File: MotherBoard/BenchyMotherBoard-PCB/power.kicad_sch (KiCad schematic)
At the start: 158 parts, among them J1 PWR-CONN, U1 TPS65400RGZT, U10 USB7206C, U11 AP2127K-3.3, U2 STM32MP157FAB1, U3 MAX15027, U4 TPS7A94, U5 ATTINY416-MNR, U6 SN74LVC1G32, U7 MAX15027, U8 74HCT2G08, U9 MAX15027

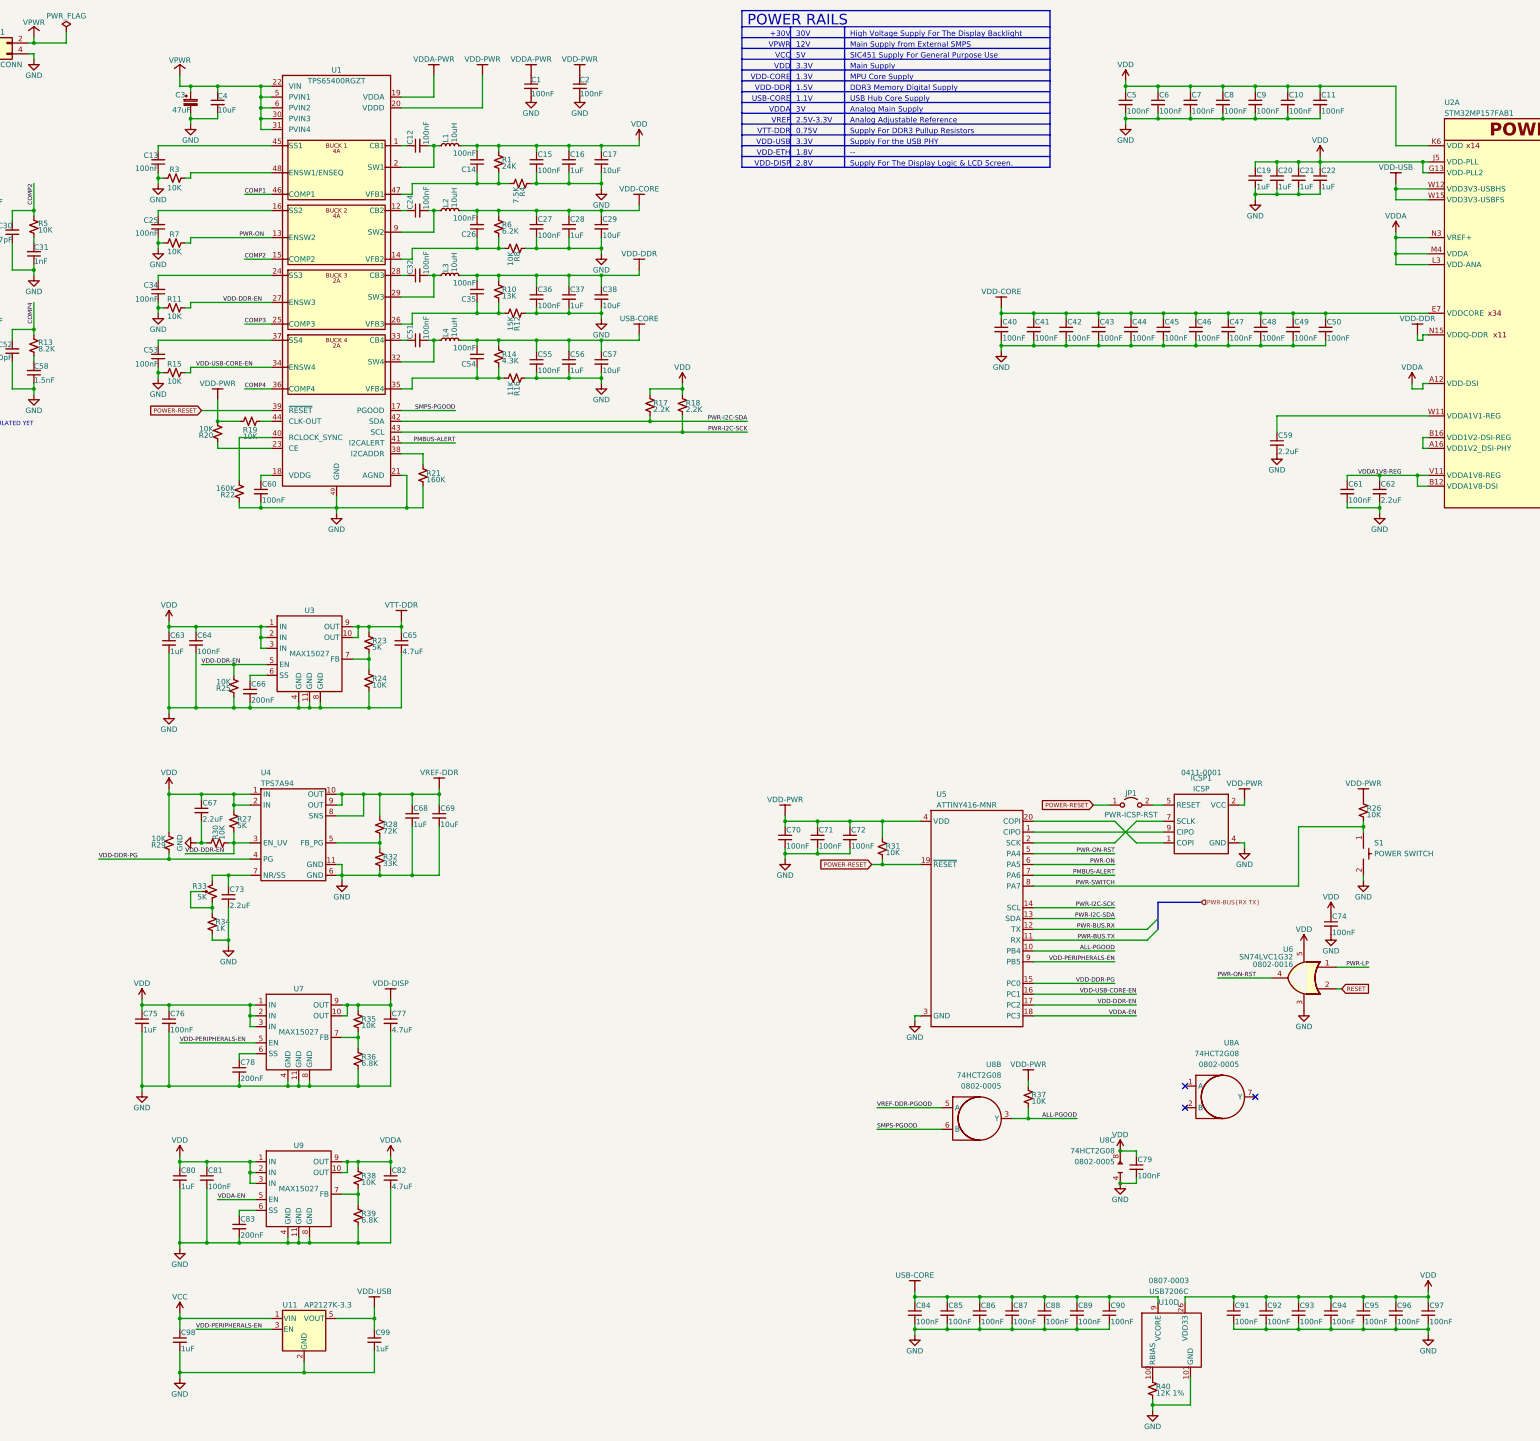
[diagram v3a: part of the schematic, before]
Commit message: (WIP) Replaced DDR VRef with reg and started layout
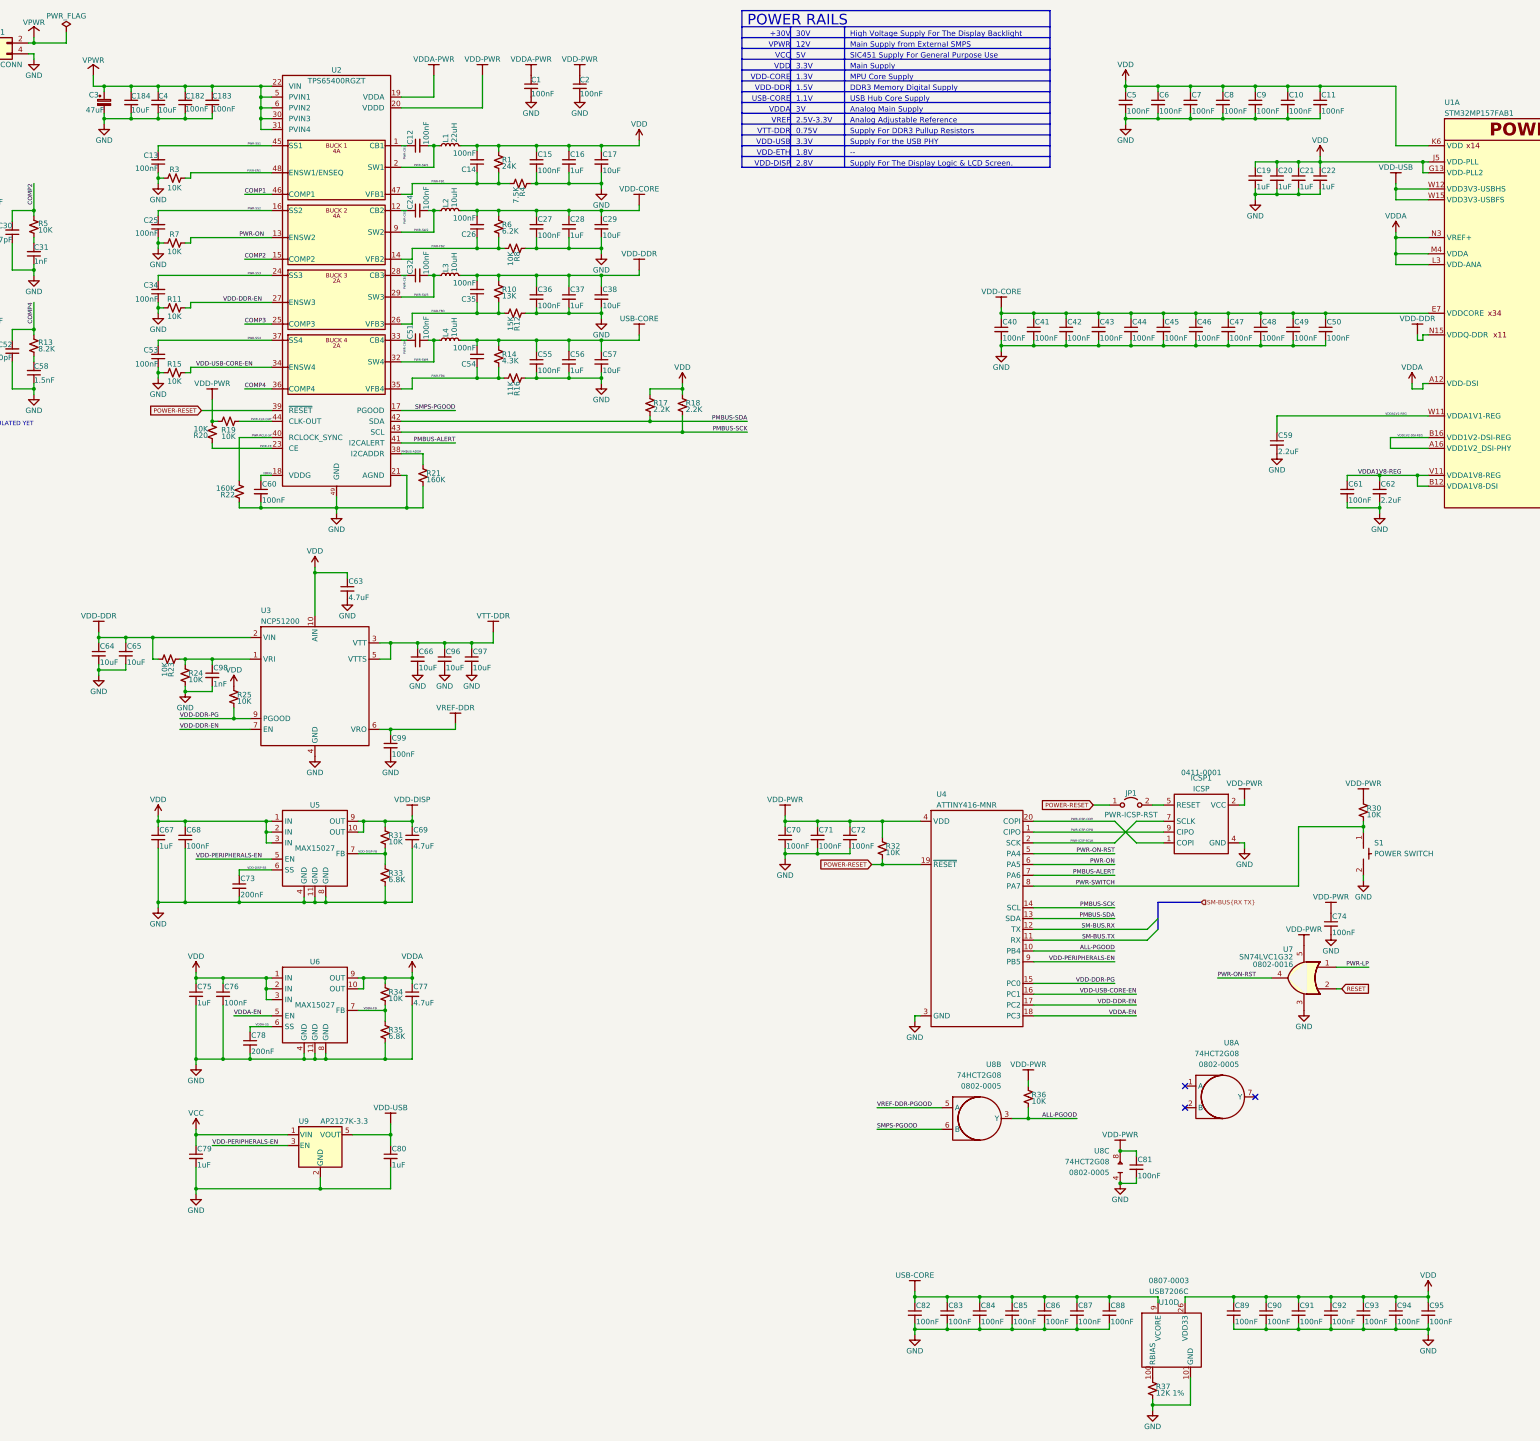
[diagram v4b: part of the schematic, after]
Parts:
- removed C67, C73: 2.2uF, Capacitor_SMD:C_0603_1608Metric, symbol Device:C_Small
- removed C68: 1uF, Capacitor_SMD:C_0603_1608Metric, symbol Device:C_Small
- removed C69: 10uF, Capacitor_SMD:C_0603_1608Metric, symbol Device:C_Small
- removed R27: 5K, Resistor_SMD:R_0402_1005Metric, symbol Device:R_Small_US
- removed R28: 72K, Resistor_SMD:R_0402_1005Metric, symbol Device:R_Small_US
- removed R29, R30: 10K, Resistor_SMD:R_0402_1005Metric, symbol Device:R_Small_US
- removed R32: 33K, Resistor_SMD:R_0402_1005Metric, symbol Device:R_Small_US
- removed R33: 5K, Daxxn_Switches:Bourns_TC33X, symbol Daxxn_Other:R_Pot_Small_US
- removed R34: 1K, Resistor_SMD:R_0402_1005Metric, symbol Device:R_Small_US
- removed U3: MAX15027, Package_DFN_QFN:DFN-10-1EP_3x3mm_P0.5mm_EP1.65x2.38mm, symbol Daxxn_Regulators:MAX15027
- removed U4: TPS7A94, Daxxn_Packages:WSON-10-1EP_3x3mm, symbol Daxxn_Regulators:TPS7A94
- added C182, C183, C99: 100nF, Capacitor_SMD:C_0402_1005Metric, symbol Device:C_Small
- added C184: 10uF, Capacitor_SMD:C_1210_3225Metric, symbol Device:C_Small
- added C96, C97: 10uF, Capacitor_SMD:C_0805_2012Metric, symbol Device:C_Small
- added C98: 1nF, Capacitor_SMD:C_0402_1005Metric, symbol Device:C_Small
- added U3: NCP51200, Package_DFN_QFN:DFN-10-1EP_3x3mm_P0.5mm_EP1.7x2.5mm, symbol Daxxn_IC:NCP51200
- C12, C14, C15, C24, C26, C27, C32, C35, C36, C51, C54, C55, C60, C74: footprint Capacitor_SMD:C_0603_1608Metric -> Capacitor_SMD:C_0402_1005Metric
- C16: footprint Capacitor_SMD:C_1210_3225Metric -> Capacitor_SMD:C_0603_1608Metric
- C63: value 1uF -> 4.7uF
- C64: value 100nF -> 10uF; footprint Capacitor_SMD:C_0603_1608Metric -> Capacitor_SMD:C_0805_2012Metric
- C65: value 4.7uF -> 10uF; footprint Capacitor_SMD:C_0603_1608Metric -> Capacitor_SMD:C_0805_2012Metric
- C66: value 200nF -> 10uF; footprint Capacitor_SMD:C_0603_1608Metric -> Capacitor_SMD:C_0805_2012Metric
- C68: renamed from C76; footprint Capacitor_SMD:C_0603_1608Metric -> Capacitor_SMD:C_0402_1005Metric
- C73: renamed from C78; footprint Capacitor_SMD:C_0603_1608Metric -> Capacitor_SMD:C_0402_1005Metric
- C76: renamed from C81; footprint Capacitor_SMD:C_0603_1608Metric -> Capacitor_SMD:C_0402_1005Metric
- C78: renamed from C83; footprint Capacitor_SMD:C_0603_1608Metric -> Capacitor_SMD:C_0402_1005Metric
- C81: renamed from C79; footprint Capacitor_SMD:C_0603_1608Metric -> Capacitor_SMD:C_0402_1005Metric
- L1: value 10uH -> 22uH
- R1, R10, R12, R14, R16, R21, R4, R6, R8: footprint Resistor_SMD:R_0603_1608Metric -> Capacitor_SMD:C_0402_1005Metric
- R23: value 5K -> 10K
- U10: footprint SnapEDA:QFN40P1200X1200X90-101N -> Daxxn_Packages:100-VQFN-GND_12X12
- renumbered C75 to C67, C77 to C69, C80 to C75, C82 to C77, C98 to C79, C99 to C80, C84 to C82, C85 to C83, C86 to C84, C87 to C85, C88 to C86, C89 to C87, C90 to C88, C91 to C89, C92 to C90, C93 to C91, C94 to C92, C95 to C93, C96 to C94, C97 to C95, R26 to R30, R35 to R31, R31 to R32, R36 to R33, R38 to R34, R39 to R35, R37 to R36, R40 to R37, U2 to U1, U1 to U2, U5 to U4, U7 to U5, U9 to U6, U6 to U7, U11 to U9
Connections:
- net GND: now also C182.1, C183.1, C184.2, C96.2, C97.2, C98.2, C99.2, U3.11 (GND), U3.4 (GND), U3.8 (GND); no longer R25.1
- net VDD: now also R25.1, U3.10 (AIN); no longer C64.1, C74.1, C81.1, U7.5, U8.8
- net VDD-DDR: now also C64.1, C65.1, R23.2, U3.2 (VIN)
- net VDD-DDR-EN: now also U3.7 (EN); no longer R25.2
- net VDD-DDR-PG: now also R25.2, U3.9 (PGOOD)
- net VDD-PWR: now also C74.1, C81.1, U7.5, U8.8
- net VPWR: now also C182.2, C183.2, C184.1
- net VREF-DDR: now also C99.1, U3.6 (VRO)
- net VTT-DDR: now also C66.1, C96.1, C97.1, U3.3 (VTT), U3.5 (VTTS); no longer C65.1, R23.1
- net PWR-CB4: now reaches C51.1, U2.33 (CB4)
- net PWR-SW4: now reaches C51.2, L4.1, U2.32 (SW4)
- net PWR-FB1: now reaches C14.1, R1.2, R4.2, U2.47 (VFB1)
- net PWR-FB2: now reaches C26.1, R6.2, R8.2, U2.14 (VFB2)
- net VDDA-FB: now reaches R34.2, R35.1, U6.7 (FB)
- net VDD1V2-DSI-REG: now reaches U1.A16 (VDD1V2_DSI-PHY), U1.B16 (VDD1V2-DSI-REG)
- net VDDA1V1-REG: now reaches C59.1, U1.W11 (VDDA1V1-REG)
- net PMBUS-ADDR: now reaches R21.1, U2.38 (I2CADDR)
- net PWR-FB4: now reaches C54.1, R14.2, R16.2, U2.35 (VFB4)
- net VDD-DISP-FB: now reaches R31.2, R33.1, U5.7 (FB)
- net VDD-DISP-SS: now reaches C73.1, U5.6 (SS)
- net at R24.1: now also R23.1, C98.1, U3.1 (VRI); no longer R23.2
- net VDDA-SS: now reaches C78.1, U6.6 (SS)
- net PWR-SW1: now reaches C12.2, L1.1, U2.2 (SW1), U2.3 (SW1), U2.4 (SW1)
- net PWR-CLK-OUT: now reaches R19.2, U2.44 (CLK-OUT)
- net PWR-FB3: now reaches C35.1, R10.2, R12.2, U2.26 (VFB3)
- net PWR-ICSP-CIPO: now reaches ICSP1.9 (CIPO), U4.1 (PA2)
- net PWR-ICSP-SCLK: now reaches ICSP1.7 (SCLK), U4.2 (PA3)
- net PWR-ICSP-COPI: now reaches ICSP1.1 (COPI), U4.20 (PA1)
- net PWR-RCLK-SY: now reaches R22.2, U2.40 (RCLOCK_SYNC)
- net VDDG: now reaches C60.1, U2.18 (VDDG)
- net PWR-SW3: now reaches C32.2, L3.1, U2.29 (SW3)
- net PWR-SS1: now reaches C13.2, U2.45 (SS1)
- net PWR-CB1: now reaches C12.1, U2.1 (CB1)
- net PWR-EN1: now reaches R3.1, U2.48 (ENSW1/ENSEQ)
- net PWR-CE: now reaches R20.1, U2.23 (CE)
- net PWR-SS2: now reaches C25.2, U2.16 (SS2)
- net PWR-SW2: now reaches C24.2, L2.1, U2.10 (SW2), U2.11 (SW2), U2.9 (SW2)
- net PWR-CB3: now reaches C32.1, U2.28 (CB3)
- net PWR-CB2: now reaches C24.1, U2.12 (CB2)
- net PWR-SS3: now reaches C34.2, U2.24 (SS3)
- net PWR-SS4: now reaches C53.2, U2.37 (SS4)
- net PWR-BUS.RX renamed SM-BUS.RX
- net PWR-BUS.TX renamed SM-BUS.TX
- net PWR-I2C-SCK renamed PMBUS-SCK
- net PWR-I2C-SDA renamed PMBUS-SDA
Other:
- moved on the sheet: C3, C4, C67, C68, C69, C73, C75, C76, C77, C78, C79, C80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
